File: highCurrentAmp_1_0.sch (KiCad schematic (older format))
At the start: 16 parts, among them U4 AD8021, U5 AD8021

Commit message: Final production board v1.0
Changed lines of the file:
@@
 EESchema Schematic File Version 2
+LIBS:MicroFLiC_DAC_1_0-rescue
 LIBS:power
 LIBS:device
@@
 	2700 2800 2800 2800
 Wire Wire Line
-	3800 2700 4200 2700
+	3800 2700 4300 2700
 Wire Wire Line
 	4100 2700 4100 4000
@@
 U 1 1 55742E4A
 P 3550 2200
+AR Path="/55742E4A" Ref="C27"  Part="1"
+AR Path="/55736CC2/55742E4A" Ref="C27"  Part="1"
 F 0 "C27" H 3600 2300 50  0000 L CNN
 F 1 "470p" H 3600 2100 50  0000 L CNN
@@
 U 1 1 55733A20
 P 3550 1900
+AR Path="/55733A20" Ref="C26"  Part="1"
+AR Path="/55736CC2/55733A20" Ref="C26"  Part="1"
 F 0 "C26" H 3600 2000 50  0000 L CNN
 F 1 "100n" H 3600 1800 50  0000 L CNN
@@
 	3200 1900 3200 2300
 Wire Wire Line
-	3350 2200 3300 2200
+	3400 2200 3300 2200
 Wire Wire Line
 	3300 2200 3200 2300
 Wire Wire Line
-	3350 1900 3250 1900
+	3400 1900 3250 1900
 Wire Wire Line
 	3250 1900 3250 2150
@@
 	3250 2150 3200 2300
 Wire Wire Line
-	3300 3350 3400 3350
+	3300 3350 3450 3350
 Wire Wire Line
 	3250 3400 3250 3650
 Wire Wire Line
-	3250 3650 3400 3650
+	3250 3650 3450 3650
 Wire Wire Line
 	3200 3100 3250 3400
@@
 U 1 1 55733A48
 P 3600 3350
+AR Path="/55733A48" Ref="C29"  Part="1"
+AR Path="/55736CC2/55733A48" Ref="C29"  Part="1"
 F 0 "C29" H 3650 3450 50  0000 L CNN
 F 1 "470p" H 3650 3250 50  0000 L CNN
@@
 U 1 1 55742E4D
 P 3600 3650
+AR Path="/55742E4D" Ref="C30"  Part="1"
+AR Path="/55736CC2/55742E4D" Ref="C30"  Part="1"
 F 0 "C30" H 3650 3750 50  0000 L CNN
 F 1 "100n" H 3650 3550 50  0000 L CNN
@@
 $EndComp
 Wire Wire Line
-	3800 3350 3900 3350
+	3750 3350 3900 3350
 Wire Wire Line
 	3900 3350 3900 3750
 Wire Wire Line
-	3800 3650 3900 3650
+	3750 3650 3900 3650
 Connection ~ 3900 3650
 Wire Wire Line
-	3750 2200 3850 2200
+	3700 2200 3850 2200
 Wire Wire Line
 	3850 1900 3850 2300
 Wire Wire Line
-	3750 1900 3850 1900
+	3700 1900 3850 1900
 Connection ~ 3850 2200
 $Comp
@@
 U 1 1 55742E50
 P 2800 2200
+AR Path="/55742E50" Ref="C25"  Part="1"
+AR Path="/55736CC2/55742E50" Ref="C25"  Part="1"
 F 0 "C25" H 2850 2300 50  0000 L CNN
 F 1 "10n" H 2850 2100 50  0000 L CNN
@@
 $EndComp
 Wire Wire Line
-	3000 2200 3100 2200
+	2950 2200 3100 2200
 Wire Wire Line
 	3100 2200 3200 2300
 Wire Wire Line
-	2600 2200 2500 2200
+	2650 2200 2500 2200
 Wire Wire Line
 	2500 2200 2500 3200
@@
 	7300 2800 7400 2800
 Wire Wire Line
-	8400 2700 8800 2700
+	8400 2700 8900 2700
 $Comp
 L C C33
 U 1 1 55742E51
 P 8150 2200
+AR Path="/55742E51" Ref="C33"  Part="1"
+AR Path="/55736CC2/55742E51" Ref="C33"  Part="1"
 F 0 "C33" H 8200 2300 50  0000 L CNN
 F 1 "470p" H 8200 2100 50  0000 L CNN
@@
 U 1 1 55742E52
 P 8150 1900
+AR Path="/55742E52" Ref="C32"  Part="1"
+AR Path="/55736CC2/55742E52" Ref="C32"  Part="1"
 F 0 "C32" H 8200 2000 50  0000 L CNN
 F 1 "100n" H 8200 1800 50  0000 L CNN
@@
 	7800 1900 7800 2300
 Wire Wire Line
-	7950 2200 7900 2200
+	8000 2200 7900 2200
 Wire Wire Line
 	7900 2200 7800 2300
 Wire Wire Line
-	7950 1900 7850 1900
+	8000 1900 7850 1900
 Wire Wire Line
 	7850 1900 7850 2150
@@
 	7900 3350 7800 3100
 Wire Wire Line
-	7900 3350 8000 3350
+	7900 3350 8050 3350
 Wire Wire Line
 	7850 3400 7850 3650
 Wire Wire Line
-	7850 3650 8000 3650
+	7850 3650 8050 3650
 Wire Wire Line
 	7800 3100 7850 3400
@@
 U 1 1 55742E53
 P 8200 3350
+AR Path="/55742E53" Ref="C35"  Part="1"
+AR Path="/55736CC2/55742E53" Ref="C35"  Part="1"
 F 0 "C35" H 8250 3450 50  0000 L CNN
 F 1 "470p" H 8250 3250 50  0000 L CNN
@@
 U 1 1 55742E54
 P 8200 3650
+AR Path="/55742E54" Ref="C36"  Part="1"
+AR Path="/55736CC2/55742E54" Ref="C36"  Part="1"
 F 0 "C36" H 8250 3750 50  0000 L CNN
 F 1 "100n" H 8250 3550 50  0000 L CNN
@@
 $EndComp
 Wire Wire Line
-	8400 3350 8500 3350
+	8350 3350 8500 3350
 Wire Wire Line
 	8500 3350 8500 3750
 Wire Wire Line
-	8400 3650 8500 3650
+	8350 3650 8500 3650
 Connection ~ 8500 3650
 Wire Wire Line
-	8350 2200 8450 2200
+	8300 2200 8450 2200
 Wire Wire Line
 	8450 1900 8450 2300
 Wire Wire Line
-	8350 1900 8450 1900
+	8300 1900 8450 1900
 Connection ~ 8450 2200
 $Comp
@@
 U 1 1 55742E57
 P 7400 2200
+AR Path="/55742E57" Ref="C31"  Part="1"
+AR Path="/55736CC2/55742E57" Ref="C31"  Part="1"
 F 0 "C31" H 7450 2300 50  0000 L CNN
 F 1 "10n" H 7450 2100 50  0000 L CNN
@@
 $EndComp
 Wire Wire Line
-	7600 2200 7700 2200
+	7550 2200 7700 2200
 Wire Wire Line
 	7700 2200 7800 2300
 Wire Wire Line
-	7200 2200 7100 2200
+	7250 2200 7100 2200
 Wire Wire Line
 	7100 2200 7100 3200
@@
 U 1 1 55738309
 P 3600 3050
+AR Path="/55738309" Ref="C28"  Part="1"
+AR Path="/55736CC2/55738309" Ref="C28"  Part="1"
 F 0 "C28" H 3650 3150 50  0000 L CNN
 F 1 "10p" H 3650 2950 50  0000 L CNN
@@
 $EndComp
 Wire Wire Line
-	3300 3050 3400 3050
-Wire Wire Line
-	3800 3050 3850 3050
+	3300 3050 3450 3050
+Wire Wire Line
+	3750 3050 3850 3050
 Wire Wire Line
 	3850 3050 3850 2800
@@
 U 1 1 557386CA
 P 8200 3050
+AR Path="/557386CA" Ref="C34"  Part="1"
+AR Path="/55736CC2/557386CA" Ref="C34"  Part="1"
 F 0 "C34" H 8250 3150 50  0000 L CNN
 F 1 "10p" H 8250 2950 50  0000 L CNN
@@
 $EndComp
 Wire Wire Line
-	7900 3050 8000 3050
+	7900 3050 8050 3050
 $Comp
 L +6V #PWR045
@@
 	3200 3100 3300 3350
 Wire Wire Line
-	8400 3050 8450 3050
+	8350 3050 8450 3050
 Wire Wire Line
 	8450 3050 8450 2800
@@
 $EndComp
 Wire Wire Line
-	5200 2700 4700 2700
-Wire Wire Line
-	9800 2700 9300 2700
+	5200 2700 4600 2700
+Wire Wire Line
+	9800 2700 9200 2700
 $Comp
 L R R24

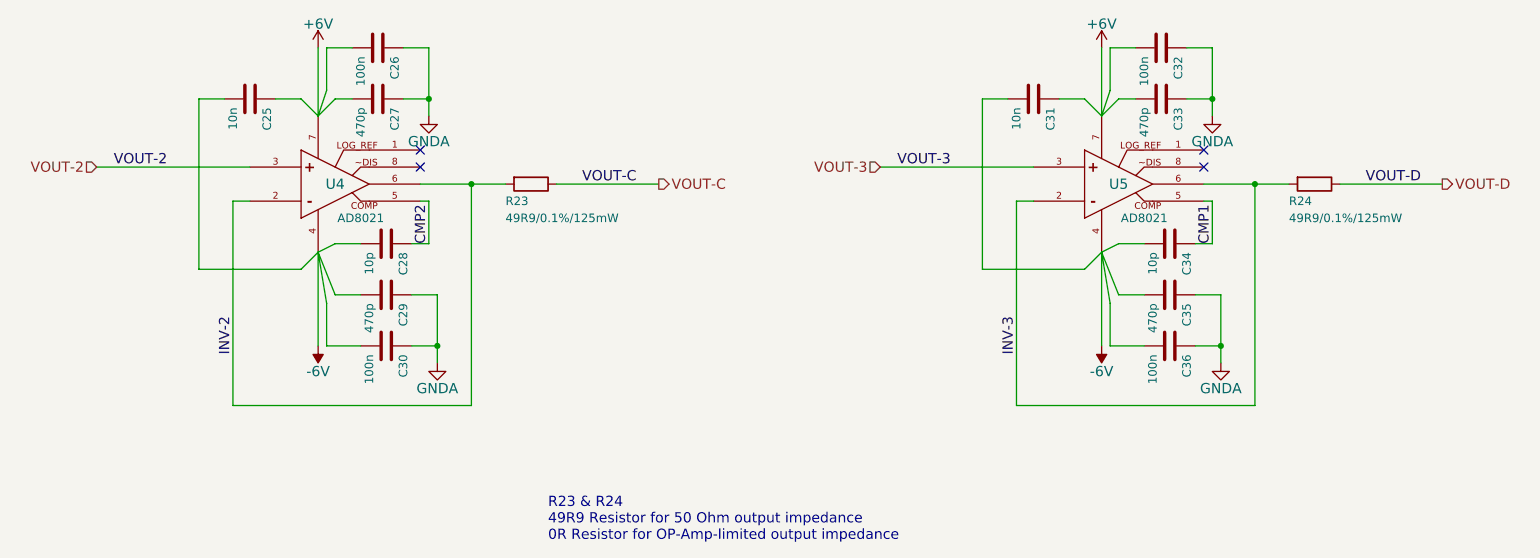
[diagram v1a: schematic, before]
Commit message: Updated part names
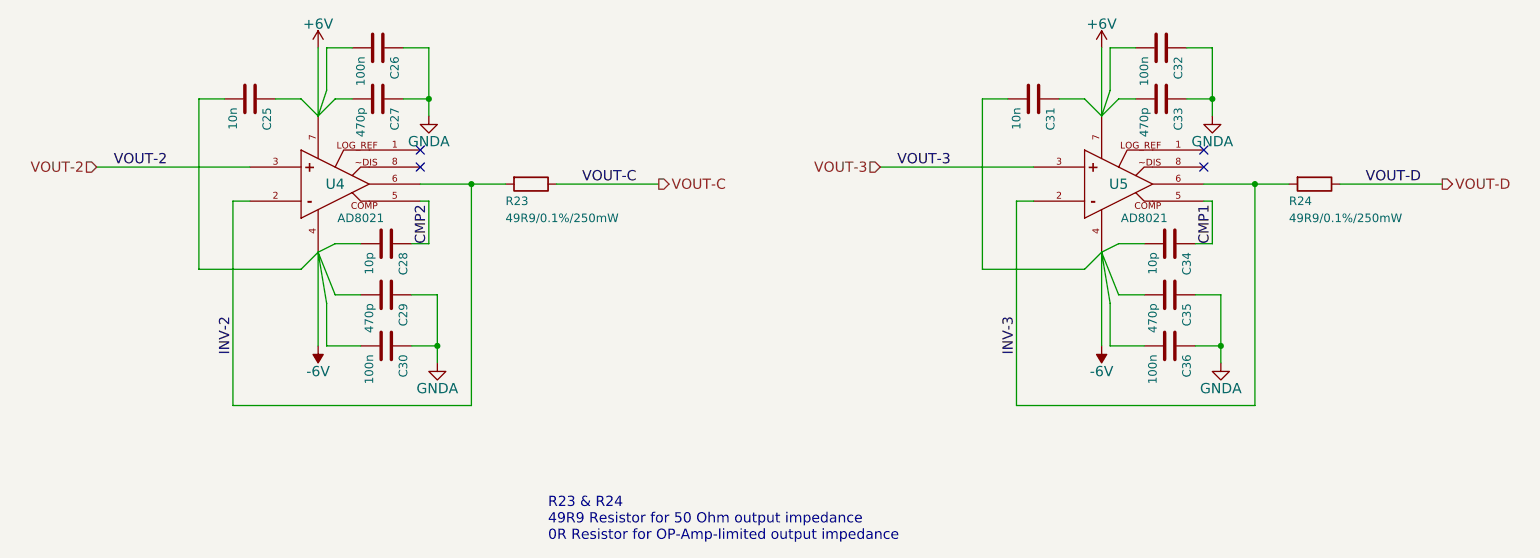
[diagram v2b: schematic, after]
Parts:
- R23, R24: value 49R9/0.1%/125mW -> 49R9/0.1%/250mW; Order Code 1502032 -> 2117023; Part Number RP73D2A49R9BTG -> RP73PF2A49R9BTDF
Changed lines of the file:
@@
 P 4450 2700
 F 0 "R23" V 4550 2550 50  0000 L CNN
-F 1 "49R9/0.1%/125mW" V 4650 2550 50  0000 L CNN
+F 1 "49R9/0.1%/250mW" V 4650 2550 50  0000 L CNN
 F 2 "Resistors_SMD:R_0805" V 4380 2700 30  0001 C CNN
 F 3 "" H 4450 2700 30  0000 C CNN
-F 4 "RP73D2A49R9BTG" V 4450 2700 60  0001 C CNN "Part Number"
+F 4 "RP73PF2A49R9BTDF" V 4450 2700 60  0001 C CNN "Part Number"
 F 5 "TE Connectivity" V 4450 2700 60  0001 C CNN "Manufacturer"
-F 6 "1502032" V 4450 2700 60  0001 C CNN "Order Code"
+F 6 "2117023" V 4450 2700 60  0001 C CNN "Order Code"
 	1    4450 2700
 	0    1    1    0
@@
 P 9050 2700
 F 0 "R24" V 9150 2550 50  0000 L CNN
-F 1 "49R9/0.1%/125mW" V 9250 2550 50  0000 L CNN
+F 1 "49R9/0.1%/250mW" V 9250 2550 50  0000 L CNN
 F 2 "Resistors_SMD:R_0805" V 8980 2700 30  0001 C CNN
 F 3 "" H 9050 2700 30  0000 C CNN
-F 4 "RP73D2A49R9BTG" V 9050 2700 60  0001 C CNN "Part Number"
+F 4 "RP73PF2A49R9BTDF" V 9050 2700 60  0001 C CNN "Part Number"
 F 5 "TE Connectivity" V 9050 2700 60  0001 C CNN "Manufacturer"
-F 6 "1502032" V 9050 2700 60  0001 C CNN "Order Code"
+F 6 "2117023" V 9050 2700 60  0001 C CNN "Order Code"
 	1    9050 2700
 	0    1    1    0
